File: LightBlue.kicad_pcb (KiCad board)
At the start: 4 copper layers, 120 x 120 mm, 260 parts, among them J1 Conn_02x05_Odd_Even, J10 Bus_M.2_Socket_M, J11 Barrel_Jack, J12 Micro_SD_Card_Det, J2 HDMI_A_2.0, J3 USB_C_Receptacle_USB2.0, J4 USB_A_Stacked, J5 SiLabs Mini Debug, J6 Conn_Coaxial, J7 Conn_02x04_Odd_Even, J8 AudioJack3, J9 RJ45_LINK-PP_LPJG0926HENL_Hor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, M1 Fan_4pin, Q1 FDMC2523P, Q2 FDMS86255, Q3 CSD17510Q5A, Q4 BCX56, Q5 CSD17510Q5A, SW1 SW_DEBUG_MODE, SW2 SW_RESET, SW3 SW_RECOVERY, SW4 SW_POWER, SW5 SW_USER, T1 Transformer_Wurth_749119550, U1 RaspberryPi-CM4Lite, U10 PCM5121PW, U11 TLV74033PDBVR, U12 TPD4EUSB30, U13 TPD4EUSB30, U14 AP64501SP-13, U15 AP64501SP-13, U16 74LVC07APW, U17 LP5569RTWR, U18 PCF85063AT, U19 RT9742GGJ5, U2 CP2102N-Axx-xQFN24, U20 TPS23734, U21 TCMT1107, U22 TL431CDBVR, U3 FSUSB42MUX, U4 FSUSB42MUX, U5 TPD4EUSB30, U6 USB2422, U7 AP2171W, U8 TPD4EUSB30, U9 SiliconLabs-MGM210P, Y1 24MHz, Y2 X32K768S301

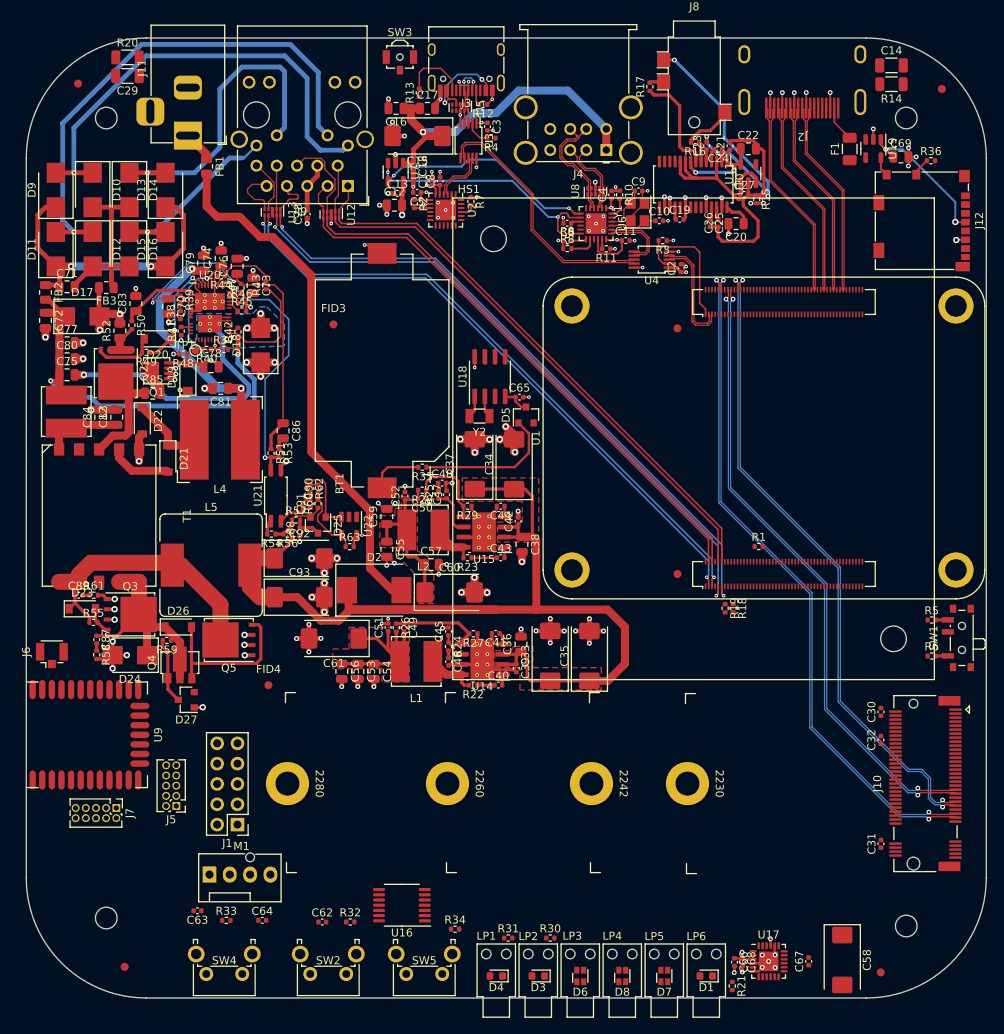
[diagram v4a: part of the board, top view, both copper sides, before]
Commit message: PCB[WIP]/SCH:
changes:
-more routing
-added poe negotiation disabled when +12V is present on the DC jack
-modified m.2 "holes"

Signed-off-by: Dominik Sliwa <dominik@sliwa.io>
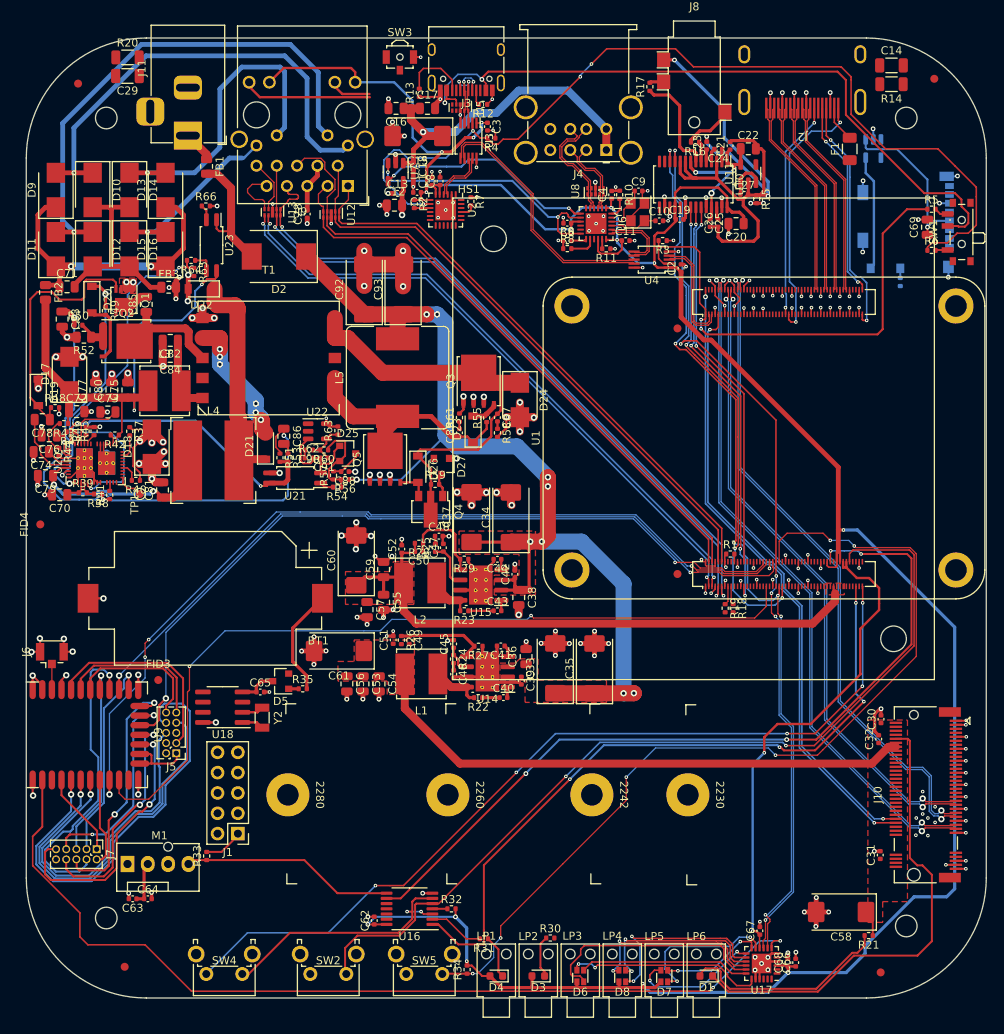
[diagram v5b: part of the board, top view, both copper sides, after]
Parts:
- added R64: 22k, Resistor_SMD:R_0402_1005Metric, F.Cu at (50.6, 57.8)
- added R65: 22k, Resistor_SMD:R_0402_1005Metric, F.Cu at (51.0, 59.2)
- added R66: 22k, Resistor_SMD:R_0402_1005Metric, F.Cu at (52.5, 51.0)
- added U23: TCMT1107, Package_SO:SOP-4_4.4x2.6mm_P1.27mm, F.Cu at (53.1, 55.9)
- J10: footprint LightBlue:TE_2199230_Bus_M.2_M_H4.2mm_P0.5mm_2280_Horizontal -> LightBlue:TE_1-2199230-3_Bus_M.2_M_H4.2mm_P0.5mm_2280_Horizontal
- J12, R36, U19: moved to B.Cu
- moved D24 58.3 mm to (91.7, 75.2), turned to -90 degrees
- moved C87 57.3 mm to (88.9, 77.5)
- moved R58 57.3 mm to (88.9, 79.4)
- moved R55 55.4 mm to (87.5, 77.5), turned to 90 degrees
- moved D23 53.8 mm to (85.8, 78.9), turned to 90 degrees
- moved U18 53.1 mm to (54.5, 113.7), turned to 180 degrees
- moved Q3 52.4 mm to (86.5, 72.9), turned to 90 degrees
- moved C89 51.7 mm to (84.2, 79.3), turned to 90 degrees
- moved R5 51.4 mm to (143.2, 51.4)
- moved R61 50.8 mm to (84.2, 77.5), turned to 90 degrees
- moved SW1 50.7 mm to (146.6, 54.2)
- moved R6 50.7 mm to (143.2, 56.5)
- moved FID3 49.6 mm to (46.5, 110.2)
- moved C65 49.1 mm to (59.2, 111.8)
- moved Y2 46.5 mm to (59.5, 115.0), turned to -90 degrees
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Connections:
- net Net-(D2-Pad2) renamed /PoE/DC_IN_F
- C70 pad 1: /PoE/VB -> /PoE/DTHR
- C72 pad 2: GND1 -> VSS
- D17 pad 2: GND1 -> VSS
- FB3 pad 2: GND1 -> VSS
- R39 pad 1: /PoE/VB -> /PoE/DTHR
- U1 pad 76: unconnected-(U1-Pad76) -> /CM4/SD.DET
- U12 pad 10: unconnected-(U12-Pad10) -> /CM4/ETH.TD1+
- U12 pad 6: unconnected-(U12-Pad6) -> /CM4/ETH.TD2+
- U12 pad 7: unconnected-(U12-Pad7) -> /CM4/ETH.TD2-
- U12 pad 9: unconnected-(U12-Pad9) -> /CM4/ETH.TD1-
- U13 pad 10: unconnected-(U13-Pad10) -> /CM4/ETH.TD3+
- U13 pad 6: unconnected-(U13-Pad6) -> /CM4/ETH.TD4+
- U13 pad 7: unconnected-(U13-Pad7) -> /CM4/ETH.TD4-
- U13 pad 9: unconnected-(U13-Pad9) -> /CM4/ETH.TD3-
- U20 pad 3: /PoE/VB -> /PoE/DTHR
- U20 pad 5: GND1 -> /PoE/APD
- U5 pad 10: unconnected-(U5-Pad10) -> /USB/USB-C.D+
- U5 pad 6: unconnected-(U5-Pad6) -> unconnected-(U5-Pad5)
- U5 pad 7: unconnected-(U5-Pad7) -> /USB/VBUS_{IN}
- U5 pad 9: unconnected-(U5-Pad9) -> /USB/USB-C.D-
- U8 pad 10: unconnected-(U8-Pad10) -> /USB/USB1.D+
- U8 pad 6: unconnected-(U8-Pad6) -> /USB/USB0.D-
- U8 pad 7: unconnected-(U8-Pad7) -> /USB/USB0.D+
- U8 pad 9: unconnected-(U8-Pad9) -> /USB/USB1.D-
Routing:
- net +3V3: track 34.1 -> 355.8 mm, vias 8 -> 15
- net GND: track 195.2 -> 316.1 mm, vias 125 -> 219
- net /802.15.4 Radio/~LED_RADIO: track 0.00 -> 117.3 mm, vias 0 -> 2
- net /SCL: track 0.00 -> 115.3 mm, vias 0 -> 6
- net /CM4/~SW_USER: track 0.00 -> 114.0 mm, vias 0 -> 6
- net /CM4/RUN_PG: track 0.00 -> 112.4 mm, vias 0 -> 2
- net /SDA: track 0.00 -> 112.0 mm, vias 0 -> 6
- net /802.15.4 Radio/Radio.RXD: track 0.00 -> 111.0 mm, vias 0 -> 4
- net /USB/MUX2_SEL: track 4.05 -> 115.0 mm, vias 1 -> 4
- net /CM4/GLOBAL_EN: track 0.00 -> 109.5 mm, vias 0 -> 5
- net /802.15.4 Radio/Radio.TXD: track 0.00 -> 102.3 mm, vias 0 -> 2
- net /CM4/~FAN_PWM: track 0.00 -> 101.4 mm, vias 0 -> 4
- net /802.15.4 Radio/Radio.RTS: track 0.00 -> 98.4 mm, vias 0 -> 2
- net /802.15.4 Radio/Radio.CTS: track 0.00 -> 96.6 mm, vias 0 -> 2
- net /CM4/~LED_PWR: track 0.00 -> 88.7 mm, vias 0 -> 4
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- added copper zone on F.Cu, net GND1
- added copper zone on In1.Cu, net VSS
- removed copper zone on In1.Cu, net GND1
- removed copper zone on B.Cu, net VSS

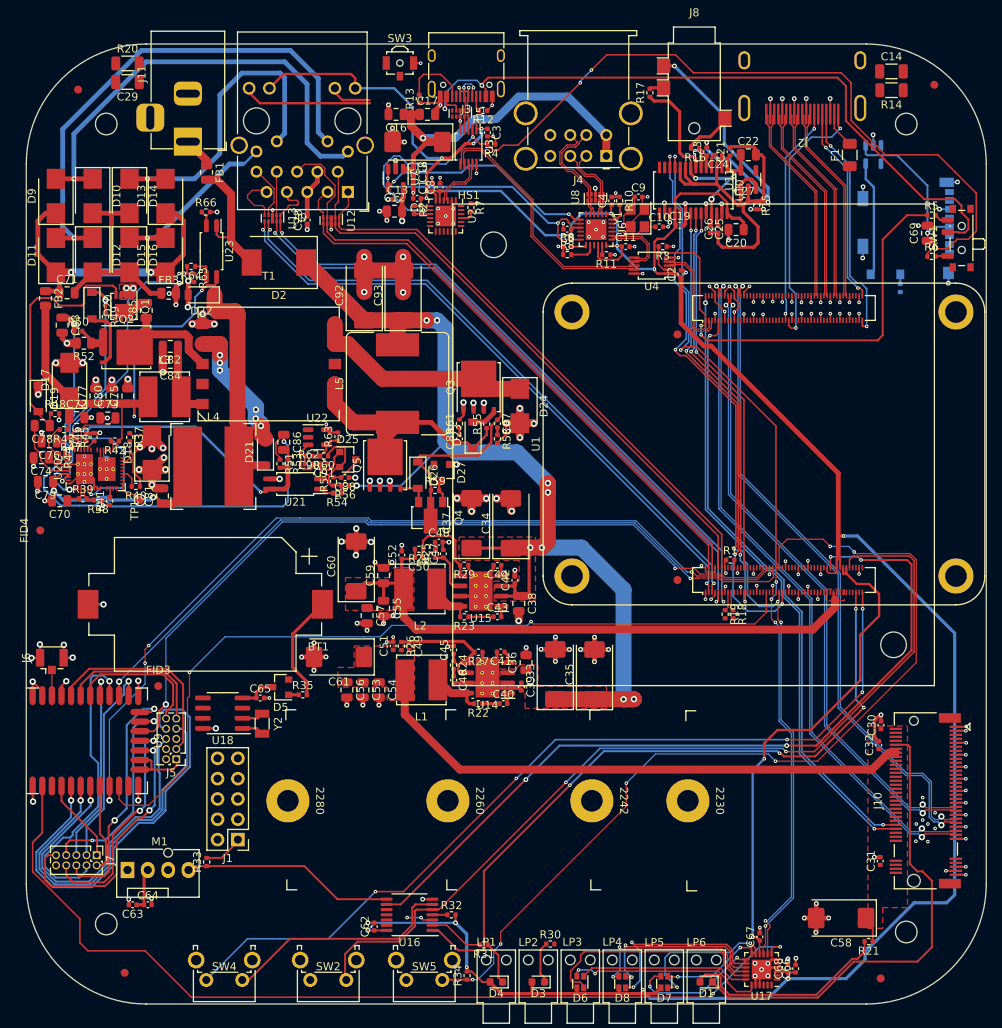
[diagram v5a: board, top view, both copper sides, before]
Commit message: PCB[WIP]: finished routing
TODO
- length matching
- review
- silkscreen

Signed-off-by: Dominik Sliwa <dominik@sliwa.io>
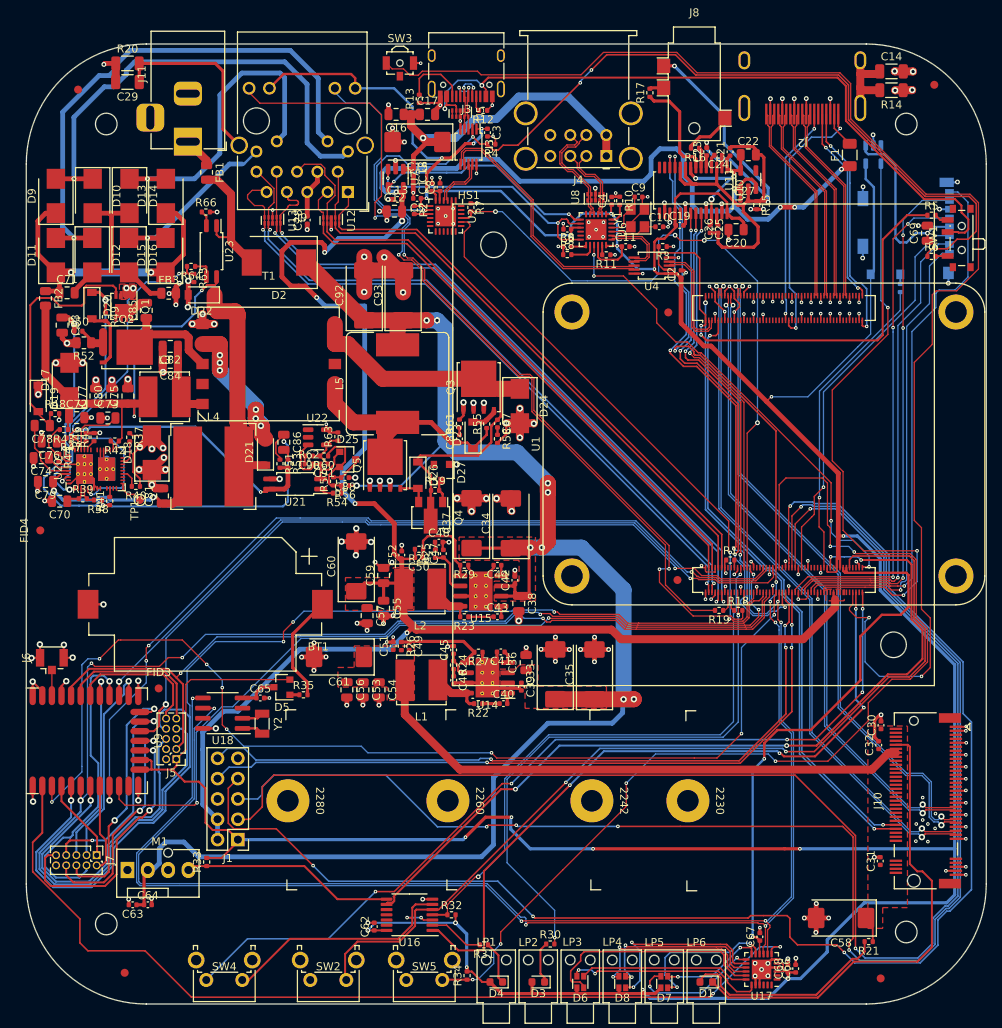
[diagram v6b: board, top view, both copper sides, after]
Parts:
- moved FID7 2.98 mm to (110.2, 63.5)
- moved R19 0.90 mm to (116.6, 100.8), turned to 180 degrees
- moved R18 0.80 mm to (119.0, 100.8), turned to 0 degrees
- moved FID3 0.30 mm to (46.5, 110.5)
- moved U13 0.27 mm to (60.8, 52.0)
- moved D5 0.15 mm to (62.0, 110.4)
- moved R35 0.09 mm to (64.7, 111.3)
- moved R52 0.05 mm to (37.2, 67.3)
- moved D13 0.05 mm to (47.5, 49.0)
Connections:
- net Net-(C29-Pad1) renamed /Ethernet/ETH_SHLD
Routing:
- net +5V: track 86.1 -> 284.4 mm, vias 1 -> 10
- net /CM4/GPIO3: track 0.00 -> 184.0 mm, vias 0 -> 5
- net /CM4/GPIO4: track 0.00 -> 182.7 mm, vias 0 -> 4
- net /CM4/GPIO2: track 0.00 -> 182.6 mm, vias 0 -> 2
- net /CM4/~RPI_BOOT: track 0.00 -> 170.7 mm, vias 0 -> 2
- net +3V3: track 355.8 -> 512.3 mm, vias 15 -> 20
- net /802.15.4 Radio/Radio.BOOT: track 0.00 -> 134.5 mm, vias 0 -> 8
- net /802.15.4 Radio/Radio.SWDIO: track 46.2 -> 158.4 mm, vias 1 -> 6
- net /SCL: track 115.3 -> 226.4 mm, vias 6 -> 8
- net /SDA: track 112.0 -> 221.2 mm, vias 6 -> 8
- net Net-(J9-Pad16): track 5.25 -> 99.1 mm, vias 0 -> 3
- net /CM4/GPIO15: track 0.00 -> 90.4 mm, vias 0 -> 3
- net /CM4/GPIO14: track 0.00 -> 90.3 mm, vias 0 -> 3
- net Net-(J9-Pad18): track 16.2 -> 104.7 mm, vias 0 -> 2
- net /802.15.4 Radio/Radio.SWCLK: track 54.4 -> 139.7 mm, vias 1 -> 4
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- added copper zone on In2.Cu, net Earth
